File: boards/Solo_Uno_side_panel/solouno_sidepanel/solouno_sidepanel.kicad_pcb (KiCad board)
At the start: 2 copper layers, 29 x 80 mm, 12 parts, among them CN1 CAN Front, CN2 CAN Back, T1 Test1, T2 Test2, T3 Test3

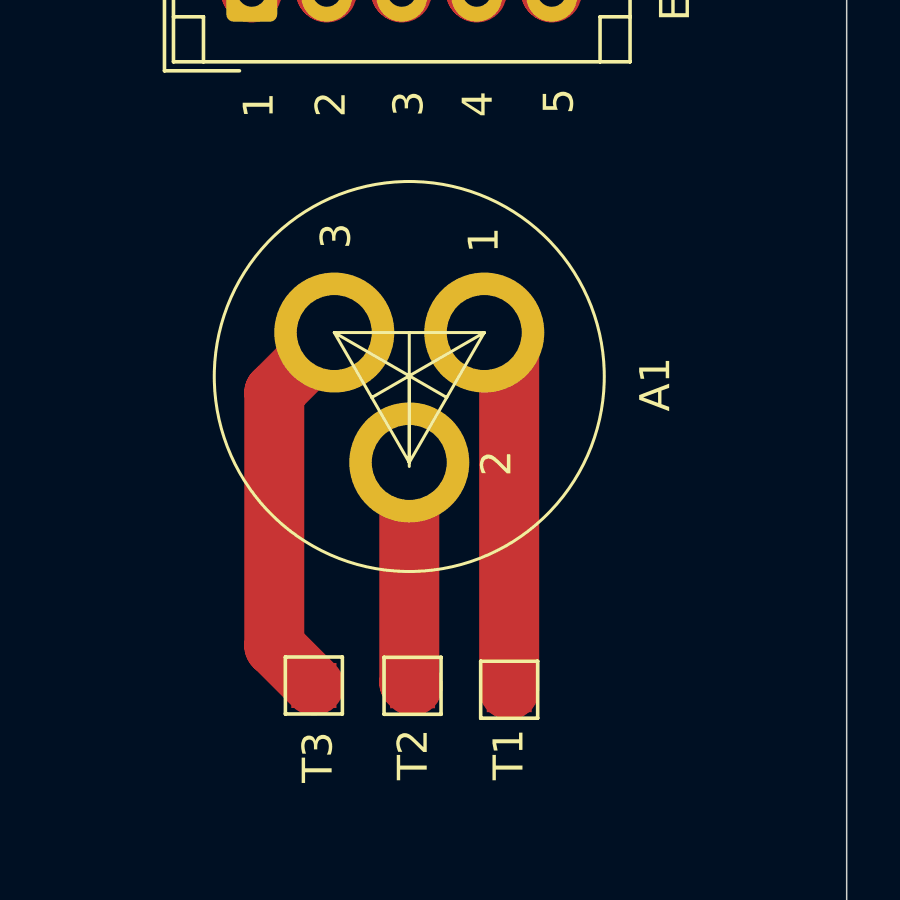
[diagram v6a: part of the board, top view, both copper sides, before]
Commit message: Fixed MotorController Board PCB and Footprint for Aviation Connector
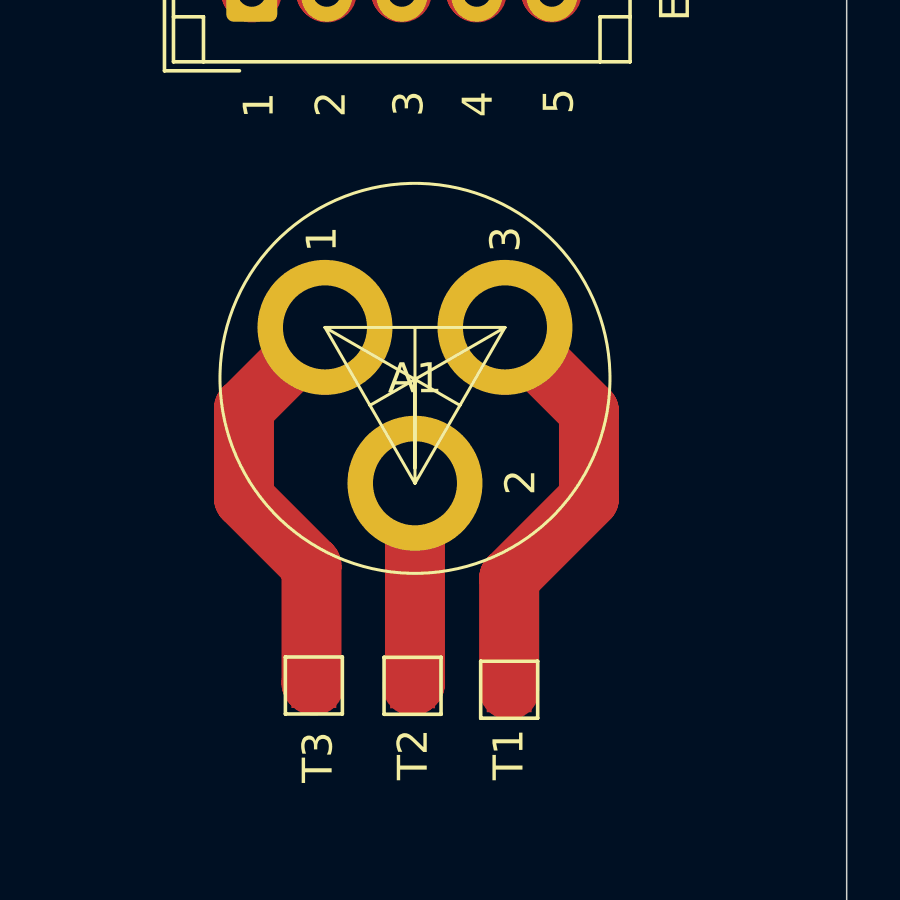
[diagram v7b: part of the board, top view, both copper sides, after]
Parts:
- A1: footprint Connector:GX-16-3 -> Robonav:GX-16-3
- moved A1 0.20 mm to (189.9, 114.2)
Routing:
- net Net-(A1-Pad1): track 12.2 -> 14.3 mm
- net Net-(A1-Pad3): track 13.1 -> 14.0 mm
- net Net-(A1-Pad2): track 7.83 -> 7.12 mm
